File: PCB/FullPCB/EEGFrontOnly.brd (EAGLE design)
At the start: 87.5 x 90 mm, 148 parts, among them IC1 ADS1299-X, J11 MICRO-SD_CARD_SOCKET, J2 USB_B_PTH, J8 JTAG, U1 LP2985-33DBVT, U10 HT7318, U11 TMS320F28335PGFA, U12 HT7333, U13 2.93V, U14 MAX811-812, U2 B0505S-1WB0505S-1W, U3 TPS60403DBVT, U4 TPS73225DBVR, U5 TPS73225DBVR, U6 TPD4E1B06DCKR, U7 TPD4E1B06DCKR, U8 TPD4E1B06DCKR, U9 HT7333, Y1 30MHz, Y2 12MHz

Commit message: update main pcb
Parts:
- added C80, C81, C82, C83, C84, C85, C86, C87, C88, C89: 0.1uF, SparkFun-Capacitors:0402
- added D2, D3: RED, SparkFun-LED:LED-0603
- added IC2: ADUM4160BRWZ, SOIC127P1032X265-16N:SOIC127P1032X265-16N
- added J12, J13, J14, J15: 455-1750-1-ND, SparkFun-Connectors:1X03
- added R34, R35, R41, R42, R43, R44: 4.7k, SparkFun-Resistors:0402
- added R36, R37, R38, R39, R40, R49, R50, R51, R52: 22, SparkFun-Resistors:0402
- added R45, R46, R47, R48: 1k, SparkFun-Resistors:0402
- added R53, R54, R55, R56: 10k, SparkFun-Resistors:0402
- added S3: (no value), switch-dil:DIP04S
- R17, R18, R19, R20: value 22 -> 0OHM
- moved C78 78.2 mm to (54.9, -13.0)
- moved C79 75.4 mm to (47.6, -13.0)
- moved Y2 71.7 mm to (51.2, -13.0)
- moved U$3 68.4 mm to (51.1, -6.10), turned to 270 degrees
- moved C54 60.4 mm to (6.13, 1.30), turned to 0 degrees
- moved R4 56.8 mm to (9.30, 0.16), turned to 0 degrees
- moved U10 56.7 mm to (4.61, -2.76), turned to 90 degrees
- moved R31 56.4 mm to (4.03, -27.7), turned to 0 degrees
- moved C53 50.7 mm to (6.13, -6.83), turned to 0 degrees
- moved R33 44.1 mm to (9.18, 1.68)
- moved R32 30.8 mm to (36.2, -33.3)
- moved C51 30.8 mm to (63.6, 22.7)
- moved C52 30.6 mm to (71.3, 22.7)
- moved U12 30.6 mm to (67.0, 24.3)
- moved C49 18.4 mm to (63.9, 29.1)
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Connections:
- removed net D+_ISO: U$3.5
- removed net D-_ISO: U$3.6
- new net D_ISO_N: R51.2, U$3.6
- new net D_ISO_P: R52.2, U$3.5
- new net D_ISO_PRE_N: IC2.11, R51.1
- new net D_ISO_PRE_P: IC2.10, R52.1
- new net D_N: J2.D-, R49.1
- new net D_P: J2.D+, R50.1
- new net N$35: R36.1, U11.96
- new net N$36: IC2.6, R49.2
- new net N$37: R37.1, U11.97
- new net N$38: R38.1, U11.98
- new net N$39: R39.1, U11.99
- new net N$40: R40.1, U11.27
- new net N$41: IC2.7, R50.2
- new net N$54: R48.1, S3.5
- new net N$55: R47.1, S3.6
- new net N$56: R46.1, S3.7
- new net N$57: R45.1, S3.8
- new net PIN: IC2.12
- new net RX: D2.C, J13.1, U$3.2, U11.20
- new net SPD: IC2.13, J15.2
- new net SPI_CS_MIRCOSD: J11.CS, R40.2, R56.1
- new net SPU: IC2.5, J14.2
- new net TX: D3.C, J13.2, U$3.3, U11.18
- new net VCC_CH340: C80.1, J12.2, R34.2, R35.2, U$3.16
- new net XA12: R41.2, S3.1, U11.169
- new net XA13: R42.2, S3.2, U11.172
- new net XA14: R43.2, S3.3, U11.173
- new net XA15: R44.2, S3.4, U11.174
- net 3.3V: now also C83.1, C84.1, IC2.14, IC2.16, J11.VCC, J12.3, J15.3, R41.1, R42.1, R43.1, R44.1, R53.2, R54.2, R55.2, R56.2
- net A1V8: now also C85.1, C86.1
- net A3V3: now also C87.1, C88.1
- net GND: now also C80.2, C83.2, C84.2, C89.2, IC2.15, IC2.9, J11.GND, J11.GND1, J11.GND3, J13.3, J15.1, R45.2, R46.2, R47.2, R48.2
- net GND-ISO: now also C81.2, C82.2, IC2.2, IC2.8, J14.1
- net GNDA: now also C85.2, C86.2, C87.2, C88.2
- net N$33: now also D2.A, R34.1; no longer U$3.2
- net N$34: now also D3.A, R35.1; no longer U$3.3
- net PWD: now also U11.114
- net RST: now also U11.113
- net SPI_CLK: now also J11.SCLK, R38.2, R55.1; no longer U11.98
- net SPI_CS: now also R39.2; no longer U11.99
- net SPI_DRDY: now also U11.26
- net SPI_MISO: now also J11.DO, R37.2, R54.1; no longer U11.97
- net SPI_MOSI: now also J11.DI, R36.2, R53.1; no longer U11.96
- net SPI_START: now also U11.28
- net VBAT: now also J12.1
- net VCC-ISO: now also C81.1, IC2.1
- net VCCIO: now also C82.1, IC2.3, IC2.4, J14.3
- net VDD3VFL: now also C89.1
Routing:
- net GND: track 309.5 -> 750.3 mm, vias 1 -> 25
- net 3.3V: track 80.2 -> 350.9 mm, vias 0 -> 21
- net 1.8V: track 73.6 -> 209.4 mm, vias 0 -> 14
- net SPI_CS_MIRCOSD: track 0.00 -> 100.3 mm, vias 0 -> 4
- net SPI_MISO: track 19.9 -> 117.5 mm, vias 0 -> 3
- net SPI_DRDY: track 25.6 -> 116.9 mm, vias 0 -> 2
- net SPI_START: track 23.3 -> 105.2 mm, vias 0 -> 2
- net GNDA: track 0.00 -> 80.9 mm, vias 0 -> 3
- net A1V8: track 0.00 -> 80.2 mm, vias 0 -> 3
- net SPI_CLK: track 27.5 -> 102.5 mm, vias 0 -> 3
- net SPI_MOSI: track 23.5 -> 95.1 mm, vias 1 -> 3
- net GND-ISO: track 87.6 -> 152.7 mm, vias 0 -> 1
- net RST: track 56.2 -> 119.4 mm, vias 2 -> 5
- net RX: track 0.00 -> 61.1 mm
- net SPI_CS: track 22.9 -> 79.8 mm, vias 2 -> 4
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- removed copper zone on layer 1, net GND-ISO

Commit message: full pcb nearly complete
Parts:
- added C90, C91: 2.2uF, SparkFun-Capacitors:0402
- added D10, D11, D4, D5, D6, D7, D8, D9: RED, SparkFun-LED:LED-0603
- added R57, R58, R59, R60, R61, R62, R63, R64: 1k, SparkFun-Resistors:0402
- added R65: 22k, SparkFun-Resistors:0402
- added U$7: (no value), xjtulogo:XJTULOGO
- moved C74 44.3 mm to (3.30, 28.7)
- moved C14 44.3 mm to (19.1, 84.3)
- moved C15 44.3 mm to (16.3, 84.1)
- moved C21 44.3 mm to (31.8, 79.6)
- moved C23 44.3 mm to (34.6, 77.3)
- moved C27 44.3 mm to (34.7, 57.6)
- moved C34 44.3 mm to (32.1, 53.6)
- moved C43 44.3 mm to (16.2, 65.0)
- moved C44 44.3 mm to (16.2, 61.7)
- moved C5 44.3 mm to (50.9, 82.1)
- moved C6 44.3 mm to (49.3, 82.1)
- moved C7 44.3 mm to (58.5, 80.4)
- moved C9 44.3 mm to (54.7, 74.9)
- moved IC1 44.3 mm to (35.2, 66.5)
- moved IC2 44.3 mm to (72.1, 57.0)
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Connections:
- net N$32 renamed EEG_REF
- new net LED1: D4.C, U11.5
- new net LED2: D5.C, U11.6
- new net LED3: D6.C, U11.7
- new net LED4: D7.C, U11.12
- new net LED5: D8.C, U11.11
- new net LED6: D9.C, U11.10
- new net LED7: D10.C, U11.21
- new net LED8: D11.C, U11.145
- new net N$32: D11.A, R64.1
- new net N$42: D10.A, R63.1
- new net N$43: D9.A, R62.1
- new net N$44: D8.A, R61.1
- new net N$45: D7.A, R60.1
- new net N$46: D6.A, R59.1
- new net N$47: D5.A, R58.1
- new net N$48: D4.A, R57.1
- new net N$49: C90.1, U11.56
- new net N$50: C91.1, U11.55
- new net N$51: R65.2, U11.57
- new net SDCARD_CD: J11.CD1, J11.CD2, U11.91
- net 3.3V: now also R57.2, R58.2, R59.2, R60.2, R61.2, R62.2, R63.2, R64.2
- net GNDA: now also C90.2, C91.2, R65.1, U11.43, U11.54
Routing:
- net 3.3V: track 350.9 -> 435.1 mm, vias 21 -> 34
- net SDCARD_CD: track 0.00 -> 62.7 mm
- net EEG_REF: track 21.6 -> 73.6 mm, vias 0 -> 8
- net LED8: track 0.00 -> 48.1 mm, vias 0 -> 4
- net LED6: track 0.00 -> 39.9 mm, vias 0 -> 2
- net GND: track 750.3 -> 789.5 mm, vias 25 -> 26
- net VCC-ISO: track 56.7 -> 95.8 mm, vias 1 -> 3
- net LED3: track 0.00 -> 36.7 mm, vias 0 -> 2
- net LED4: track 0.00 -> 36.6 mm, vias 0 -> 2
- net LED5: track 0.00 -> 36.5 mm, vias 0 -> 2
- net XA14: track 38.6 -> 74.7 mm, vias 0 -> 2
- net LED2: track 0.00 -> 36.1 mm, vias 0 -> 2
- net XA15: track 40.6 -> 76.1 mm, vias 0 -> 2
- net LED1: track 0.00 -> 35.0 mm, vias 0 -> 2
- net XA13: track 37.7 -> 72.1 mm, vias 0 -> 2
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- removed copper zone on layer 1, net AGND
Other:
- board size 87.5 x 90 mm -> 87.5 x 90.9 mm
- board text added: "EEG-DSP Joint PCB"
- board text added: "Jingjie Li - XJTU BME- 11 MAY 2019"
- board text removed: "EEG-FrontOnly PCB"
- board text removed: "Jingjie Li - 25 MAR 2019"

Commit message: full pcb nearly complete
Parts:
- added J16, J17: (no value), SparkFun-Connectors:1X02
- added U$10, U$11, U$8, U$9: (no value), SparkFun-Hardware:STAND-OFF
- moved U2 13.0 mm to (51.0, 86.6)
- moved J3 13.0 mm to (64.3, 88.8)
- moved J4 13.0 mm to (67.1, 88.8)
- moved J15 0.13 mm to (85.6, 52.2)
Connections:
- net GND: now also J16.2
- net GND-ISO: now also J16.1
- net VBATPRE: now also J17.2
- net VCC-ISO: now also J17.1
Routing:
- net VCC-ISO: track 95.8 -> 84.0 mm
- net GND-ISO: track 123.3 -> 115.7 mm
- net GND: track 789.5 -> 783.1 mm
- net VBATPRE: track 39.6 -> 42.3 mm
- net N$1: track 6.03 -> 6.61 mm
- net VBAT: track 146.0 -> 145.5 mm
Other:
- board size 87.5 x 90.9 mm -> 87.4 x 92.6 mm
- board text added: "PWR- ISO"
- board text removed: "ISO-PINS"
- board text removed: "ISOLATION BARRIER"
- board text removed: "USB_PWR"

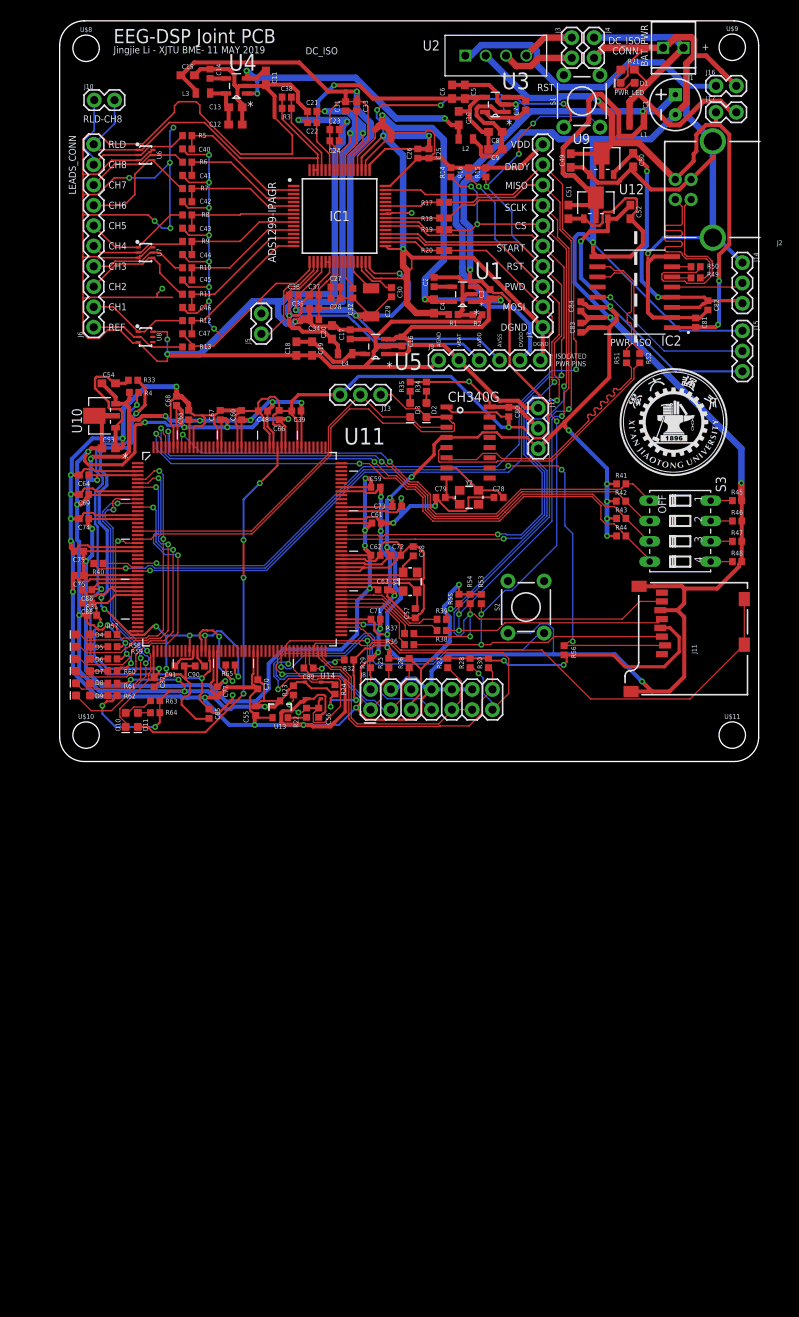
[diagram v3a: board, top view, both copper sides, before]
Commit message: GND copper cover
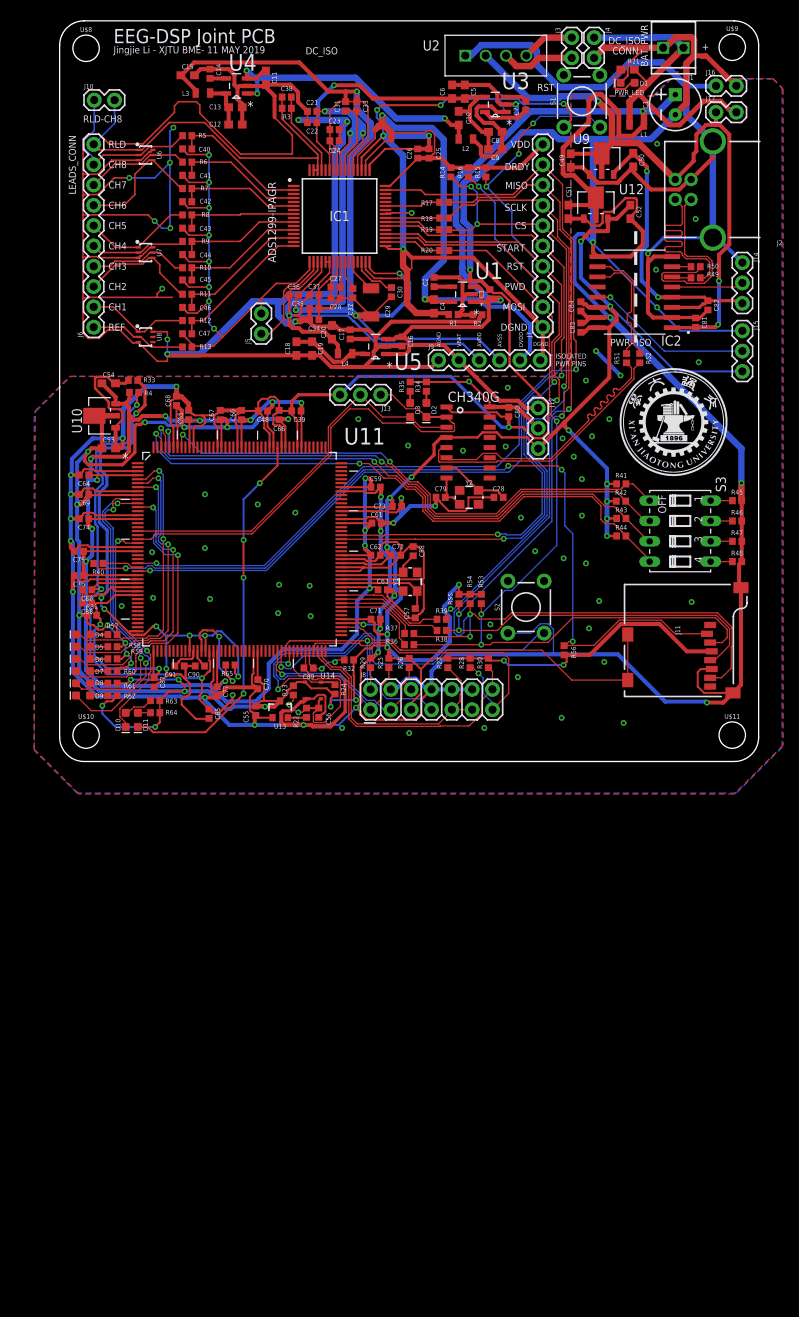
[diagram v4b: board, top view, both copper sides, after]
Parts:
- moved J11 20.9 mm to (70.9, 6.48), turned to 270 degrees
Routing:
- net SDCARD_CD: track 62.7 -> 44.2 mm
- net SPI_MISO: track 117.5 -> 134.7 mm
- net SPI_CLK: track 102.5 -> 117.1 mm
- net SPI_MOSI: track 95.1 -> 108.3 mm
- net SPI_CS_MIRCOSD: track 100.6 -> 107.8 mm
- net GND: track 783.1 -> 787.9 mm, vias 26 -> 73
- net 3.3V: track 435.0 -> 436.0 mm
- added copper zone on layer 1, net GND
- added copper zone on layer 16, net GND
